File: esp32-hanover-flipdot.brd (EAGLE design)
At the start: 45.1 x 25.4 mm, 28 parts, among them J1 DC-005, J2 HANOVER, J3 FTDI, Q1 NCE3407A, Q2 S9013, U1 ESP32-PICO-D4, U2 CJA1117B-3.3-SOT89, U3 LM2576SX-5.0/NOPB

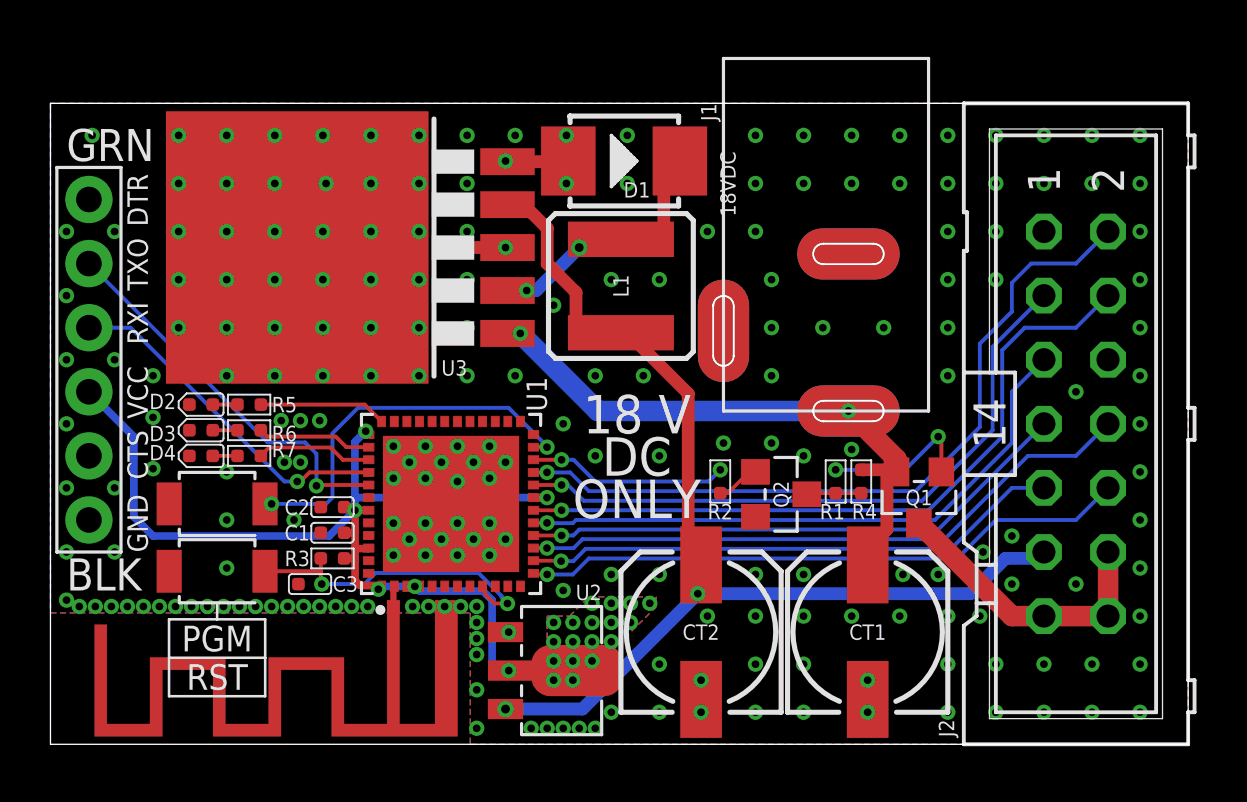
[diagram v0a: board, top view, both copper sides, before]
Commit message: Change buck converter from LM7576-5.0 to AP63205, change antenna
Change buck converter from LM7576-5.0 to AP63205, which uses drastically less space and switches at a higher frequency thus requiring smaller passives, and does not require a schottky diode.

Change antenna to a larger inverted-F antenna which has more isotropic gain thus makes placement of the board less of a factor in Wi-Fi performance.
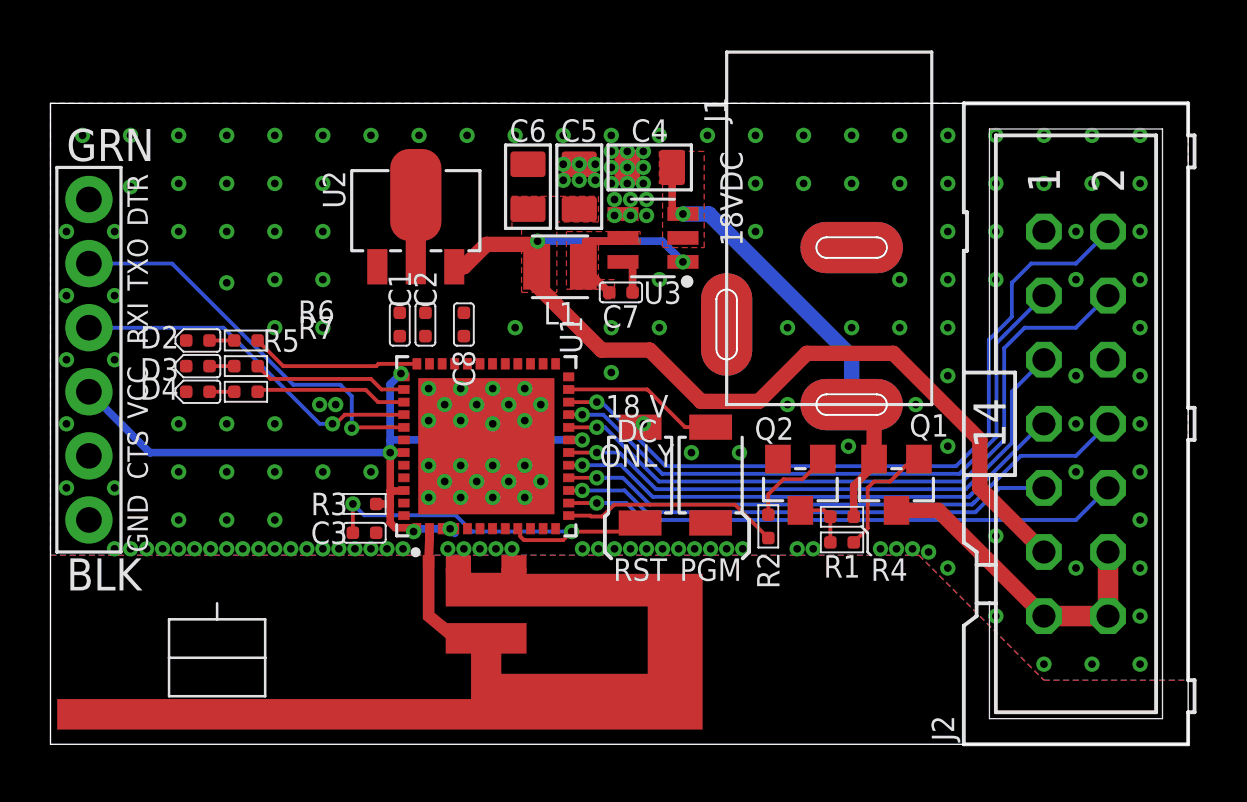
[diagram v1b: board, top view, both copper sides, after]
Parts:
- removed CT1: 100UF, OPL_Capacitor:ELECTRO-SMD-C-6MM
- removed CT2: 220UF, OPL_Capacitor:ELECTRO-SMD-C-6MM
- removed D1: 28V-5A, OPL_Discrete_Semiconductor:DO-214AA
- added C4: 10uf, OPL_Capacitor_No_Thermals:C0805
- added C5, C6: 22uf, OPL_Capacitor_No_Thermals:C0805
- added C7: 100nf, OPL_Capacitor:C0402
- added C8: 10uf, OPL_Capacitor:C0402
- E1: value ANTENNA-GROUNDEDTRACE-15.2MM -> ANTENNA-GROUNDEDTRACE-25.7MM; device SparkFun-RF:TRACE_ANTENNA_2.4GHZ_15.2MM -> SparkFun-RF-GND-Extended:TRACE_ANTENNA_2.4GHZ_25.7MM
- L1: value 220uH -> 4.7uH; device SparkFun-Coils:CR54 -> TDK VLS201610HBX-1:INDC2016X100N
- U3: value LM2576SX-5.0/NOPB -> AP63205WU-7; device LM2576 (1):TO263-5 -> Diodes_Inc_AP6320:SOT95P280X100-6N
- moved PGM 19.6 mm to (26.2, 10.7), turned to 90 degrees
- moved U2 18.7 mm to (14.5, 20.8), turned to 0 degrees
- moved RST 17.2 mm to (23.4, 10.7), turned to 270 degrees
- moved U3 11.6 mm to (23.9, 20.1), turned to 180 degrees
- moved C1 8.68 mm to (13.8, 16.6), turned to 180 degrees
- moved C2 8.12 mm to (14.9, 16.6), turned to 180 degrees
- moved C3 2.96 mm to (12.4, 8.38), turned to 270 degrees
- moved E1 2.68 mm to (15.0, 7.49)
- moved U1 2.68 mm to (17.3, 11.8)
- moved R2 2.61 mm to (28.4, 8.64), turned to 0 degrees
- moved D3 2.54 mm to (5.84, 15.0)
- moved D4 2.54 mm to (5.84, 14.0)
- moved R6 2.54 mm to (7.75, 15.0)
- moved R7 2.54 mm to (7.75, 14.0)
- moved D2 2.54 mm to (5.84, 16.0)
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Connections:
- new net N$8: C7.2, L1.1, U3.5
- net +18V: now also C4.2, U3.2, U3.3; no longer CT1.+, U3.1
- net +3V3: now also C8.2
- net +5V: now also C5.2, C6.2, L1.2, U3.1; no longer CT2.+, L1.P$2, U3.4
- net GND: now also C4.1, C5.1, C6.1, C8.1, E1.GND2, U3.4; no longer CT1.-, CT2.-, D1.+, U3.3, U3.5
- net GPIO12: now also J2.5; no longer J2.4
- net GPIO13: now also J2.4; no longer J2.3
- net GPIO14: now also J2.7; no longer J2.5
- net GPIO15: now also J2.3; no longer J2.2
- net GPIO2: now also J2.2; no longer R2.2
- net GPIO25: now also J2.10; no longer J2.9
- net GPIO26: now also J2.9; no longer J2.8
- net GPIO27: now also J2.8; no longer J2.7
- net GPIO33: now also R2.2; no longer J2.10
- net N$4: now also C7.1, U3.6; no longer D1.-, L1.P$1, U3.2
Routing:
- net GPIO2: track 7.95 -> 29.2 mm, vias 2 -> 1
- net GPIO33: track 24.2 -> 8.78 mm, vias 1 -> 0
- net +3V3: track 44.6 -> 32.6 mm, vias 24 -> 5
- net GPIO0: track 15.4 -> 6.24 mm, vias 2 -> 0
- net N$4: track 10.2 -> 1.59 mm, vias 2 -> 0
- net +5V: track 44.3 -> 37.9 mm
- net GPIO12: track 28.3 -> 22.7 mm
- net GPIO26: track 24.8 -> 19.6 mm
- net GPIO15: track 29.9 -> 24.9 mm
- net +18V: track 23.9 -> 18.9 mm, vias 2 -> 1
- net GND: track 4.40 -> 0.00 mm, vias 224 -> 198
- net N$8: track 0.00 -> 4.08 mm
- net GPIO14: track 24.1 -> 20.6 mm
- net EN: track 12.7 -> 15.7 mm
- net N$3: track 1.75 -> 3.55 mm
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- added copper zone on layer 1, net +18V
- added copper zone on layer 1, net +5V
- added copper zone on layer 1, net N$8
- removed copper zone on layer 1, net +3V3
- removed copper zone on layer 16, net +3V3
